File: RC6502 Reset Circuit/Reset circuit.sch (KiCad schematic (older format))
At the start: 12 parts, among them J1 CONN_01X39, J2 XTAL Enable, SW1 RESET, U1 NE555, U2 74LS04, X1 1MHz

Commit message: Exported files
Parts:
- added C4: 100nF, Capacitors_THT:C_Disc_D3.0mm_W1.6mm_P2.50mm, symbol C
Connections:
- net GND: now also C4.2
- net VCC: now also C4.1
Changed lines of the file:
@@
 U 1 1 5909CC66
 P 6100 2925
-F 0 "R1" V 6180 2925 50  0000 C CNN
+F 0 "R1" V 6025 2925 50  0000 C CNN
 F 1 "1M" V 6100 2925 50  0000 C CNN
 F 2 "Resistors_THT:R_Axial_DIN0207_L6.3mm_D2.5mm_P10.16mm_Horizontal" V 6030 2925 50  0001 C CNN
@@
 U 1 1 5909D4EB
 P 8025 3225
-F 0 "R2" V 8105 3225 50  0000 C CNN
+F 0 "R2" V 7950 3225 50  0000 C CNN
 F 1 "47k" V 8025 3225 50  0000 C CNN
 F 2 "Resistors_THT:R_Axial_DIN0207_L6.3mm_D2.5mm_P10.16mm_Horizontal" V 7955 3225 50  0001 C CNN
@@
 	1    0    0    -1
 $EndComp
+Text GLabel 1100 1850 3    60   Output ~ 0
+GND
+Text GLabel 1100 1100 1    60   Input ~ 0
+VCC
+$Comp
+L C C4
+U 1 1 591A9FB0
+P 1100 1475
+F 0 "C4" H 1125 1575 50  0000 L CNN
+F 1 "100nF" H 1125 1375 50  0000 L CNN
+F 2 "Capacitors_THT:C_Disc_D3.0mm_W1.6mm_P2.50mm" H 1138 1325 50  0001 C CNN
+F 3 "" H 1100 1475 50  0001 C CNN
+	1    1100 1475
+	1    0    0    -1
+$EndComp
+Wire Wire Line
+	1100 1325 1100 1100
+Wire Wire Line
+	1100 1625 1100 1850
 $EndSCHEMATC

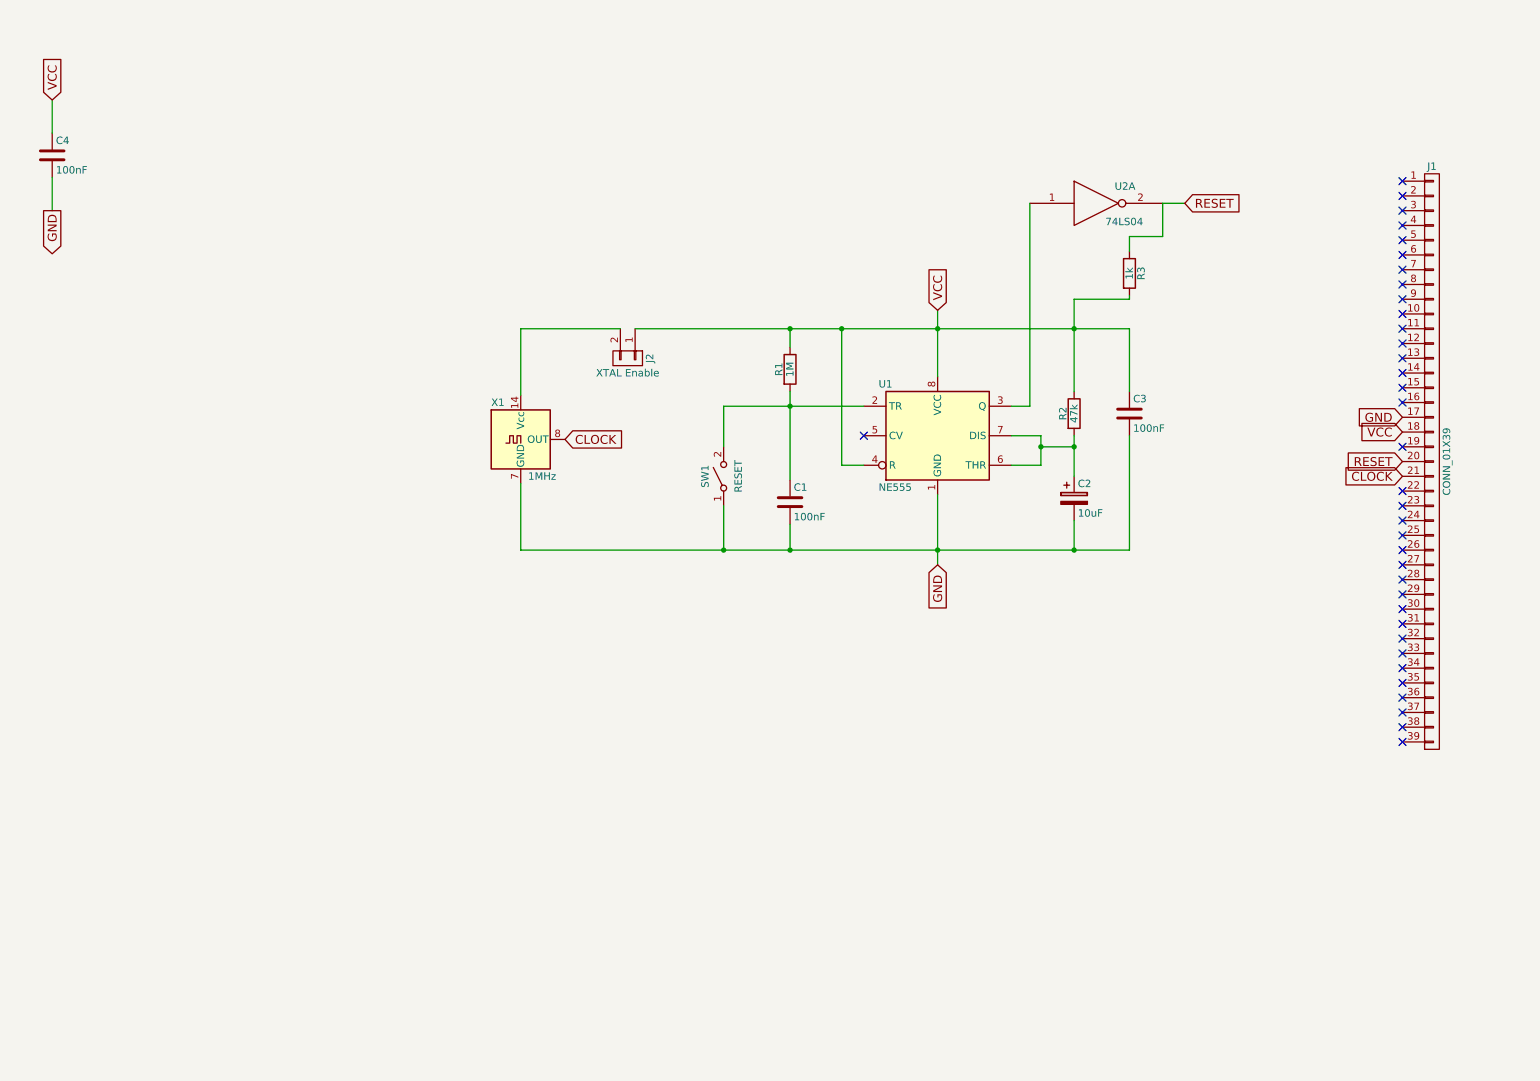
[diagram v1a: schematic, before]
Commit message: Reset circuit revision B
Fixed floating inputs on hex inverter (needed when using HCT), added 74HCT74 in order to allow clock division by 2 and 4 (in case missing matching TTL quartz crystal or want even slower clock than stock).
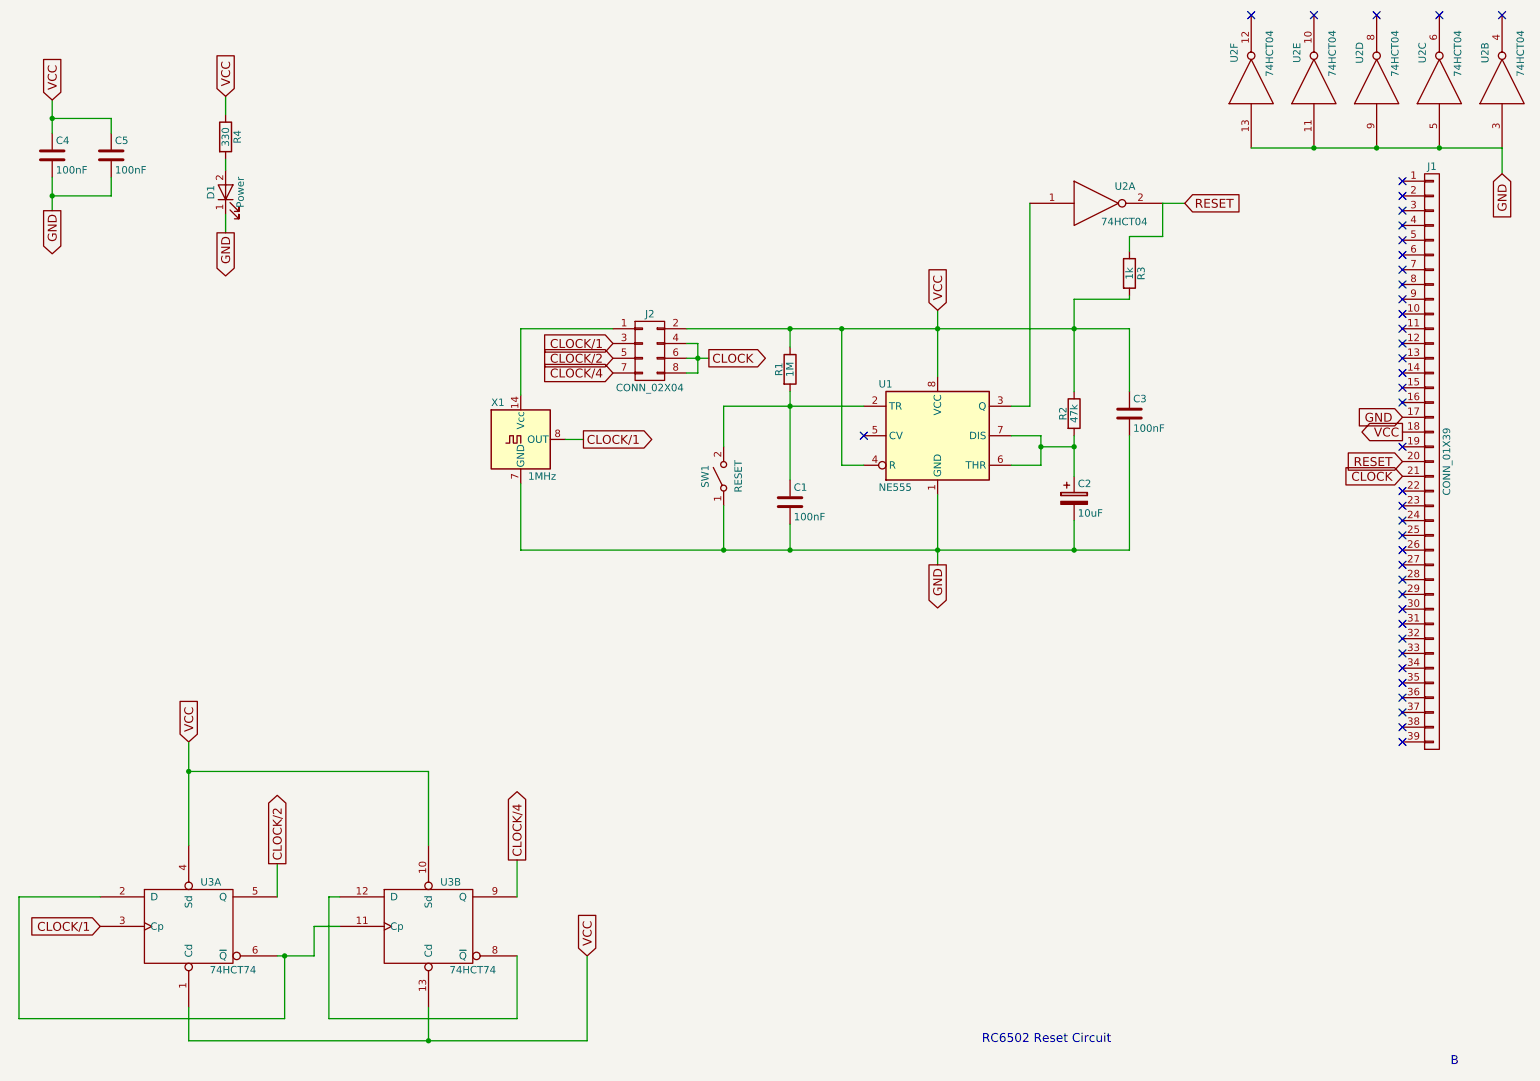
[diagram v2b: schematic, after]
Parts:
- removed J2: XTAL Enable, Pin_Headers:Pin_Header_Angled_1x02_Pitch2.54mm, symbol CONN_01X02
- added C5: 100nF, Capacitors_THT:C_Disc_D4.7mm_W2.5mm_P5.00mm, symbol C
- added D1: Power, LEDs:LED_D5.0mm, symbol LED
- added J2: CONN_02X04, Pin_Headers:Pin_Header_Straight_2x04_Pitch2.54mm, symbol CONN_02X04
- added R4: 330, Resistors_THT:R_Axial_DIN0207_L6.3mm_D2.5mm_P10.16mm_Horizontal, symbol R
- added unit 2 of U2
- added unit 3 of U2
- added unit 4 of U2
- added unit 5 of U2
- added unit 6 of U2
- added U3: 74HCT74, Housings_DIP:DIP-14_W7.62mm_Socket, symbol 74LS74
- C1, C3, C4: footprint Capacitors_THT:C_Disc_D3.0mm_W1.6mm_P2.50mm -> Capacitors_THT:C_Disc_D4.7mm_W2.5mm_P5.00mm
- U2: value 74LS04 -> 74HCT04
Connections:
- net CLOCK: now also J2.4 (P4), J2.6 (P6), J2.8 (P8); no longer X1.8 (OUT)
- net GND: now also C5.2, D1.1 (K), U2.11, U2.13, U2.3, U2.5, U2.7 (GND), U2.7 (GND), U2.7 (GND), U2.7 (GND), U2.7 (GND), U2.9, U3.7 (GND), U3.7 (GND)
- net VCC: now also C5.1, J2.2 (P2), R4.1, U2.14 (VCC), U2.14 (VCC), U2.14 (VCC), U2.14 (VCC), U2.14 (VCC), U3.1 (Cd), U3.10 (Sd), U3.13 (Cd), U3.14 (VCC), U3.14 (VCC), U3.4 (Sd)
- net at X1.14 (Vcc): now also J2.1 (P1)
- new net: U3.11 (Cp), U3.2 (D), U3.6 (~Q)
- new net: U3.12 (D), U3.8 (~Q)
- new net: D1.2 (A), R4.2
- new net CLOCK/1: J2.3 (P3), U3.3 (Cp), X1.8 (OUT)
- new net CLOCK/2: J2.5 (P5), U3.5 (Q)
- new net CLOCK/4: J2.7 (P7), U3.9 (Q)
- no-connect marks 36 -> 41
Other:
- note added: "B"
- note added: "RC6502 Reset Circuit"

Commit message: VDU basic IO mapping start
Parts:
- SW1: symbol SW_SPST -> SW_SPST-RESCUE-Reset_circuit
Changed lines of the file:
@@
 EESchema Schematic File Version 2
+LIBS:Reset circuit-rescue
 LIBS:power
 LIBS:device
@@
 RESET
 $Comp
-L SW_SPST SW1
+L SW_SPST-RESCUE-Reset_circuit SW1
 U 1 1 5909ECDD
 P 5650 3650
@@
 	6600 3575 6450 3575
 Wire Wire Line
-	6450 2650 6450 3575
+	6450 3575 6450 2650
 Connection ~ 6450 2650
 Wire Wire Line
